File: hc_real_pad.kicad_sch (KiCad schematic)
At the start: 0 parts

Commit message: did schematic
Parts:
- added D1, D10, D11, D12, D13, D14, D15, D16, D17, D18, D2, D3, D4, D5, D6, D7, D8, D9: 1N4148, Diode_THT:D_DO-35_SOD27_P7.62mm_Horizontal, symbol Diode:1N4148
- added D19, D20, D21, D22, D23, D24, D25, D26, D27, D28, D29, D30, D31, D32, D33, D34: WS2812B, LED_SMD:LED_WS2812B_PLCC4_5.0x5.0mm_P3.2mm, symbol LED:WS2812B
- added J1: OLED_DISPLAY, symbol Connector:Conn_01x04_Pin
- added SW1, SW10, SW11, SW12, SW13, SW14, SW15, SW16, SW2, SW3, SW4, SW5, SW6, SW7, SW8, SW9: SW_Push_45deg, symbol Switch:SW_Push_45deg
- added SW17, SW18: RotaryEncoder_Switch, symbol Device:RotaryEncoder_Switch
- added U1: MOUDLE-SEEEDUINO-XIAO, symbol XIAO_RP2040:MOUDLE-SEEEDUINO-XIAO
- added U3: MCP23017_SP, Package_DIP:DIP-28_W7.62mm, symbol Interface_Expansion:MCP23017_SP
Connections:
- new net: D4.2 (A), SW4.2
- new net: D10.2 (A), SW10.2
- new net: D17.2 (A), SW17.A
- new net: D25.2 (DOUT), D26.4 (DIN)
- new net: D24.2 (DOUT), D25.4 (DIN)
- new net: D13.2 (A), SW13.2
- new net: D29.2 (DOUT), D30.4 (DIN)
- new net: D14.2 (A), SW14.2
- new net: D31.2 (DOUT), D32.4 (DIN)
- new net: D26.2 (DOUT), D31.4 (DIN)
- new net: D1.2 (A), SW1.2
- new net: D12.2 (A), SW12.2
- new net: D15.2 (A), SW15.2
- new net: D23.2 (DOUT), D24.4 (DIN)
- new net: D16.2 (A), SW16.2
- new net: D33.2 (DOUT), D34.4 (DIN)
- new net: D32.2 (DOUT), D33.4 (DIN)
- new net: D5.2 (A), SW5.2
- new net: D7.2 (A), SW7.2
- new net: D9.2 (A), SW9.2
- new net: D11.2 (A), SW11.2
- new net: D2.2 (A), SW2.2
- new net: D19.2 (DOUT), D20.4 (DIN)
- new net: D19.4 (DIN), D34.2 (DOUT)
- new net: D28.2 (DOUT), D29.4 (DIN)
- new net: D27.2 (DOUT), D28.4 (DIN)
- new net: D22.2 (DOUT), D27.4 (DIN)
- new net: D3.2 (A), SW3.2
- new net: D8.2 (A), SW8.2
- new net: D20.2 (DOUT), D21.4 (DIN)
- new net: D18.2 (A), SW18.A
- new net: D6.2 (A), SW6.2
- new net: D21.2 (DOUT), D22.4 (DIN)
- new net +3.3V: U1.12 (3V3), U3.9 (VDD)
- new net COL0: SW1.1, SW13.1, SW5.1, SW9.1, U3.21 (GPA0)
- new net COL1: SW10.1, SW14.1, SW2.1, SW6.1, U3.22 (GPA1)
- new net COL2: SW11.1, SW15.1, SW3.1, SW7.1, U3.23 (GPA2)
- new net COL3: SW12.1, SW16.1, SW4.1, SW8.1, U3.24 (GPA3)
- new net COL4: SW17.B, SW18.B
- new net ENCSWA0: SW17.S2, U1.2 (PA4_A1_D1)
- new net ENCSWA1: SW18.S2, U1.4 (PA11_A3_D3)
- new net ENCSWB0: SW17.S1, U1.3 (PA10_A2_D2)
- new net ENCSWB1: SW18.S1, U1.7 (PB08_A6_D6_TX)
- new net GND: D19.3 (VSS), D20.3 (VSS), D21.3 (VSS), D22.3 (VSS), D23.3 (VSS), D24.3 (VSS), D25.3 (VSS), D26.3 (VSS), D27.3 (VSS), D28.3 (VSS), D29.3 (VSS), D30.3 (VSS), D31.3 (VSS), D32.3 (VSS), D33.3 (VSS), D34.3 (VSS), J1.4 (Pin_4), SW17.C, SW18.C, U1.13 (GND), U3.10 (VSS)
- new net INTA: U1.1 (PA02_A0_D0), U3.20 (INTA)
- new net ROW0: D1.1 (K), D17.1 (K), D18.1 (K), D2.1 (K), D3.1 (K), D4.1 (K), U3.1 (GPB0)
- new net ROW1: D5.1 (K), D6.1 (K), D7.1 (K), D8.1 (K), U3.2 (GPB1)
- new net ROW2: D10.1 (K), D11.1 (K), D12.1 (K), D9.1 (K), U3.3 (GPB2)
- new net ROW3: D13.1 (K), D14.1 (K), D15.1 (K), D16.1 (K), U3.4 (GPB3)
- new net SCL: J1.2 (Pin_2), U1.6 (PA9_A5_D5_SCL), U3.12 (SCK)
- new net SDA: J1.1 (Pin_1), U1.5 (PA8_A4_D4_SDA), U3.13 (SDA)
- new net VCC: D19.1 (VDD), D20.1 (VDD), D21.1 (VDD), D22.1 (VDD), D23.1 (VDD), D24.1 (VDD), D25.1 (VDD), D26.1 (VDD), D27.1 (VDD), D28.1 (VDD), D29.1 (VDD), D30.1 (VDD), D31.1 (VDD), D32.1 (VDD), D33.1 (VDD), D34.1 (VDD), J1.3 (Pin_3), U1.14 (5V)
- new net WS2812B: D23.4 (DIN), U1.11 (PA6_A10_D10_MOSI)
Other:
- note added: "Encoders"
- note added: "IO Expander"
- note added: "LED Matrix"
- note added: "MCU"
- note added: "OLED Display"
- note added: "Switch Matrix"

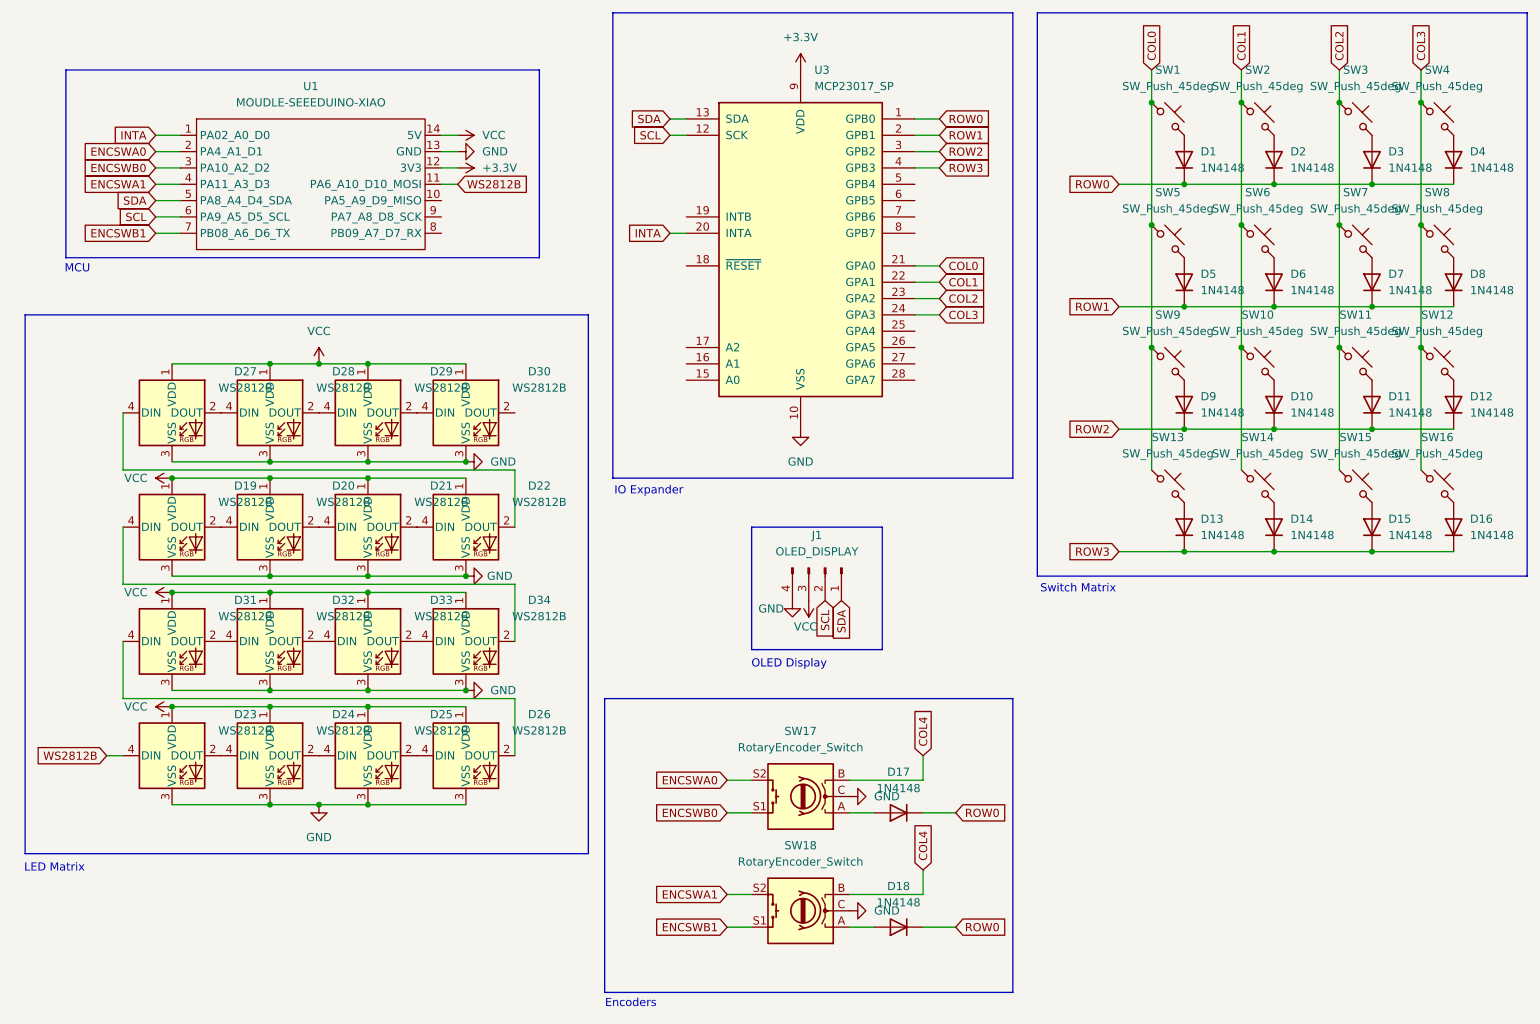
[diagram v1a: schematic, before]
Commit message: fixed issues with schematic
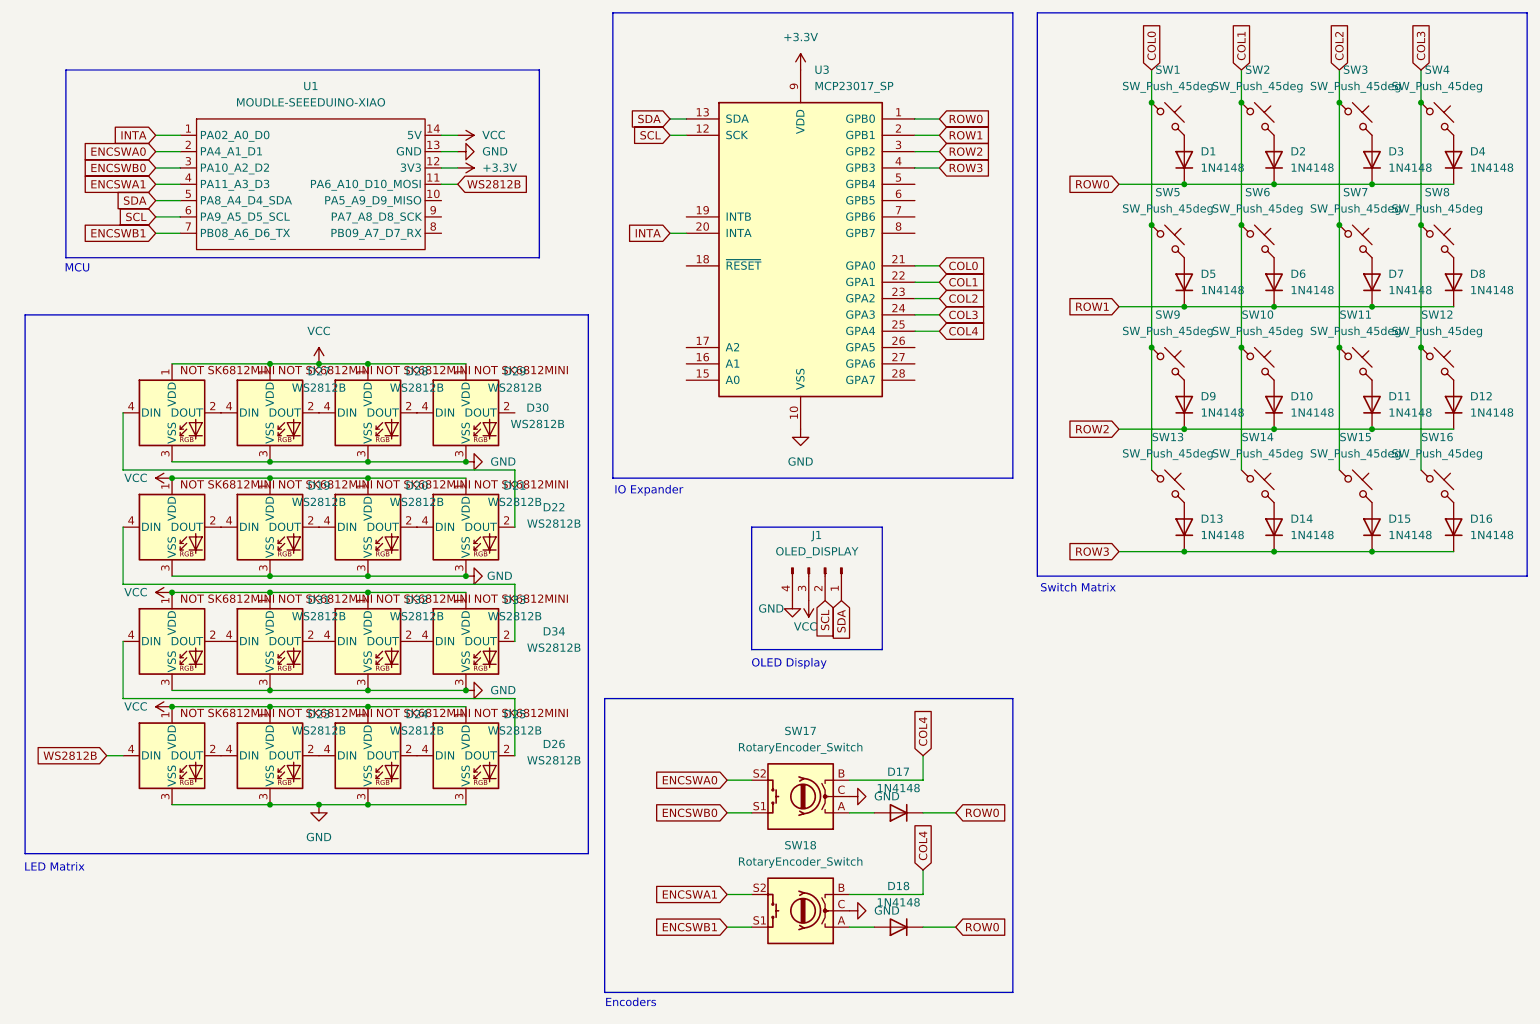
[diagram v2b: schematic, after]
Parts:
- D19, D20, D21, D22, D23, D24, D25, D26, D27, D28, D29, D30, D31, D32, D33, D34: footprint LED_SMD:LED_WS2812B_PLCC4_5.0x5.0mm_P3.2mm -> footprints:SK6812MINI-E_fixed; symbol LED:WS2812B -> SK6812MINI-E:SK6812MINI-E
- J1: footprint (none) -> Display:SSD1306-0.91-OLED-4pin-128x32
- SW1, SW10, SW11, SW12, SW13, SW14, SW15, SW16, SW2, SW3, SW4, SW5, SW6, SW7, SW8, SW9: footprint (none) -> Button_Switch_Keyboard:SW_Cherry_MX_1.00u_PCB
- SW17: footprint (none) -> Encoders:RotaryEncoder_Alps_EC11E-Switch_Vertical_H20mm
- SW18: footprint (none) -> Rotary_Encoder:RotaryEncoder_Alps_EC11E-Switch_Vertical_H20mm
- U1: footprint (none) -> footprints:XIAO-Generic-Hybrid-14P-2.54-21X17.8MM
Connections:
- net COL4: now also U3.25 (GPA4)

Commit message: finished making the pcb
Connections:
- net GND: now also J1.1 (Pin_1); no longer J1.4 (Pin_4)
- net SCL: now also J1.3 (Pin_3); no longer J1.2 (Pin_2)
- net SDA: now also J1.4 (Pin_4); no longer J1.1 (Pin_1)
- net VCC: now also J1.2 (Pin_2); no longer J1.3 (Pin_3)
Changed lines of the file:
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@@
 	(global_label "SDA"
 		(shape input)
-		(at 144.78 106.68 270)
+		(at 137.16 106.68 270)
 		(fields_autoplaced yes)
 		(effects
@@
 		)
 		(property "Intersheetrefs" "${INTERSHEET_REFS}"
-			(at 144.78 113.2333 90)
+			(at 137.16 113.2333 90)
 			(effects
 				(font
@@
 	(global_label "SCL"
 		(shape input)
-		(at 142.24 106.68 270)
+		(at 139.7 106.68 270)
 		(fields_autoplaced yes)
 		(effects
@@
 		)
 		(property "Intersheetrefs" "${INTERSHEET_REFS}"
-			(at 142.24 113.1728 90)
+			(at 139.7 113.1728 90)
 			(effects
 				(font
@@
 	(symbol
 		(lib_id "power:GND")
-		(at 137.16 106.68 0)
+		(at 144.78 106.68 0)
 		(unit 1)
 		(exclude_from_sim no)
@@
 		(dnp no)
 		(property "Reference" "#PWR09"
-			(at 137.16 113.03 0)
+			(at 144.78 113.03 0)
 			(effects
 				(font
@@
 		)
 		(property "Value" "GND"
-			(at 133.858 107.95 0)
+			(at 147.828 107.95 0)
 			(effects
 				(font
@@
 		)
 		(property "Footprint" ""
-			(at 137.16 106.68 0)
+			(at 144.78 106.68 0)
 			(effects
 				(font
@@
 		)
 		(property "Datasheet" ""
-			(at 137.16 106.68 0)
+			(at 144.78 106.68 0)
 			(effects
 				(font
@@
 		)
 		(property "Description" "Power symbol creates a global label with name \"GND\" , ground"
-			(at 137.16 106.68 0)
+			(at 144.78 106.68 0)
 			(effects
 				(font
@@
 	(symbol
 		(lib_id "power:VCC")
-		(at 139.7 106.68 180)
+		(at 142.24 106.68 180)
 		(unit 1)
 		(exclude_from_sim no)
@@
 		(dnp no)
 		(property "Reference" "#PWR08"
-			(at 139.7 102.87 0)
+			(at 142.24 102.87 0)
 			(effects
 				(font
@@
 		)
 		(property "Value" "VCC"
-			(at 139.192 110.744 0)
+			(at 143.002 110.744 0)
 			(effects
 				(font
@@
 		)
 		(property "Footprint" ""
-			(at 139.7 106.68 0)
+			(at 142.24 106.68 0)
 			(effects
 				(font
@@
 		)
 		(property "Datasheet" ""
-			(at 139.7 106.68 0)
+			(at 142.24 106.68 0)
 			(effects
 				(font
@@
 		)
 		(property "Description" "Power symbol creates a global label with name \"VCC\""
-			(at 139.7 106.68 0)
+			(at 142.24 106.68 0)
 			(effects
 				(font
